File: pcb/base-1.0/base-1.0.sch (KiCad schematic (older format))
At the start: 80 parts, among them J101 USB_B_Micro, J102 UART, J103 74984104400, J104 Jack-DC, J105 USB_GPIO, J106 Raspberry_Pi_2_3, Q101 BC817, Q102 BC817, Q103 DMP2305U-7, SW101 SW_Push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

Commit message: o Finding more components. o Refreshing generated files.
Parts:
- Q101, Q102: mpn (none) -> BC817,235
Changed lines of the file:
@@
 F 2 "Package_TO_SOT_SMD:SOT-23" H 9200 2225 50  0001 L CIN
 F 3 "https://assets.nexperia.com/documents/data-sheet/BC817_SER.pdf" H 9000 2300 50  0001 L CNN
+F 4 "BC817,235" H 9000 2300 50  0001 C CNN "mpn"
 	1    9000 2300
 	1    0    0    1
@@
 F 2 "Package_TO_SOT_SMD:SOT-23" H 9200 1525 50  0001 L CIN
 F 3 "https://assets.nexperia.com/documents/data-sheet/BC817_SER.pdf" H 9000 1600 50  0001 L CNN
+F 4 "BC817,235" H 9000 1600 50  0001 C CNN "mpn"
 	1    9000 1600
 	1    0    0    -1

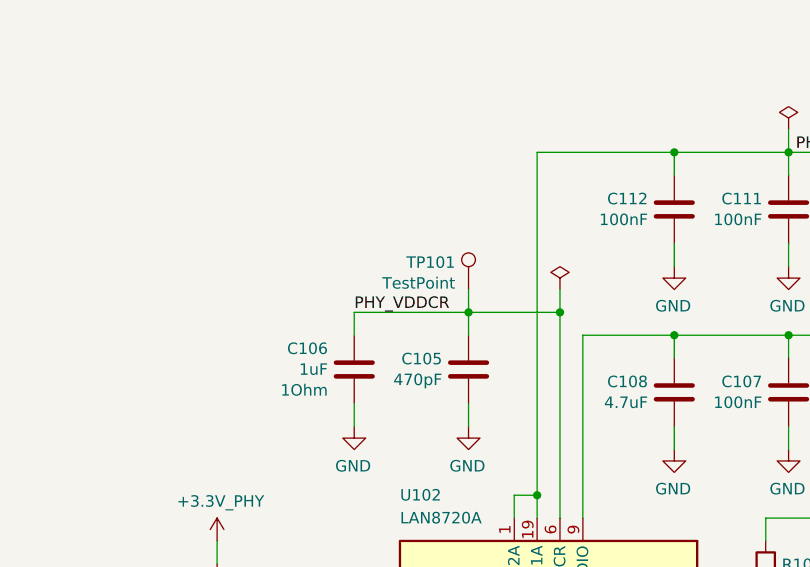
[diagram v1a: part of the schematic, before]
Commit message: o Selecting more parts, fixing footprints.
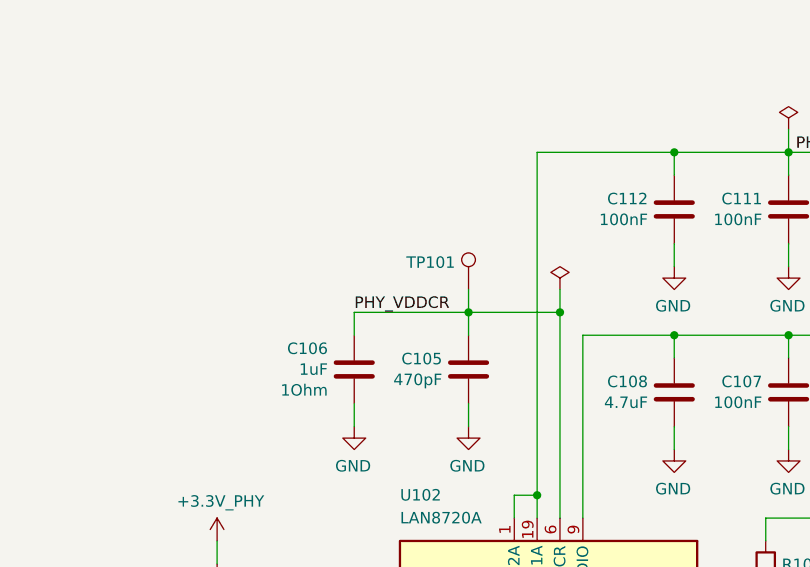
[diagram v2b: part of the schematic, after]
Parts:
- C104: footprint IPC-7351-CAPC:CAPC_1005x015 -> IPC-7351-CAPC:CAPC_4532x040
- C120, C121: footprint IPC-7351-CAPC:CAPC_1005x015 -> IPC-7351-CAPC:CAPC_2012x040
- FB101, FB102: mpn (none) -> FBMJ2125HS250NT
- TP101: value TestPoint -> PHY_VDDCR
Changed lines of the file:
@@
 F 0 "C104" H 2015 10841 50  0000 L CNN
 F 1 "1nF" H 2015 10750 50  0000 L CNN
-F 2 "IPC-7351-CAPC:CAPC_1005x015" H 1938 10600 50  0001 C CNN
+F 2 "IPC-7351-CAPC:CAPC_4532x040" H 1938 10600 50  0001 C CNN
 F 3 "~" H 1900 10750 50  0001 C CNN
 F 4 "2kV" H 2015 10659 50  0000 L CNN "Voltage"
@@
 Wire Wire Line
 	6000 7700 6000 7600
-$Comp
-L Connector:TestPoint TP101
-U 1 1 5DDF6049
-P 4600 7400
-F 0 "TP101" H 4658 7518 50  0000 L CNN
-F 1 "TestPoint" H 4658 7427 50  0000 L CNN
-F 2 "TestPoint:TestPoint_Pad_1.5x1.5mm" H 4800 7400 50  0001 C CNN
-F 3 "~" H 4800 7400 50  0001 C CNN
-	1    4600 7400
-	-1   0    0    -1
-$EndComp
 Connection ~ 4600 7500
 Wire Wire Line
@@
 F 4 "2A" V 6850 6800 50  0001 C CNN "I"
 F 5 "50mOhm" V 6850 6800 50  0001 C CNN "DCR"
+F 6 "FBMJ2125HS250NT" V 6850 6800 50  0001 C CNN "mpn"
 	1    6850 6800
 	0    -1   1    0
@@
 F 2 "Inductor_SMD:L_0402_1005Metric" V 1330 1200 50  0001 C CNN
 F 3 "~" H 1400 1200 50  0001 C CNN
+F 4 "FBMJ2125HS250NT" V 1400 1200 50  0001 C CNN "mpn"
 	1    1400 1200
 	0    1    1    0
@@
 F 0 "C120" H 13215 6441 50  0000 L CNN
 F 1 "100nF" H 13215 6350 50  0000 L CNN
-F 2 "IPC-7351-CAPC:CAPC_1005x015" H 13138 6200 50  0001 C CNN
+F 2 "IPC-7351-CAPC:CAPC_2012x040" H 13138 6200 50  0001 C CNN
 F 3 "" H 13100 6350 50  0000 C CNN
 F 4 "C3" H 13100 6350 50  0001 C CNN "ta_ref"
@@
 F 0 "C121" H 13215 8541 50  0000 L CNN
 F 1 "100nF" H 13215 8450 50  0000 L CNN
-F 2 "IPC-7351-CAPC:CAPC_1005x015" H 13138 8300 50  0001 C CNN
+F 2 "IPC-7351-CAPC:CAPC_2012x040" H 13138 8300 50  0001 C CNN
 F 3 "" H 13100 8450 50  0000 C CNN
 F 4 "C3" H 13100 8450 50  0001 C CNN "ta_ref"
@@
 	0    1    -1   0
 $EndComp
+$Comp
+L Connector:TestPoint TP101
+U 1 1 5DDF6049
+P 4600 7400
+F 0 "TP101" H 4658 7518 50  0000 L CNN
+F 1 "PHY_VDDCR" H 4658 7427 50  0001 L CNN
+F 2 "TestPoint:TestPoint_Pad_1.5x1.5mm" H 4800 7400 50  0001 C CNN
+F 3 "~" H 4800 7400 50  0001 C CNN
+	1    4600 7400
+	-1   0    0    -1
+$EndComp
 $EndSCHEMATC

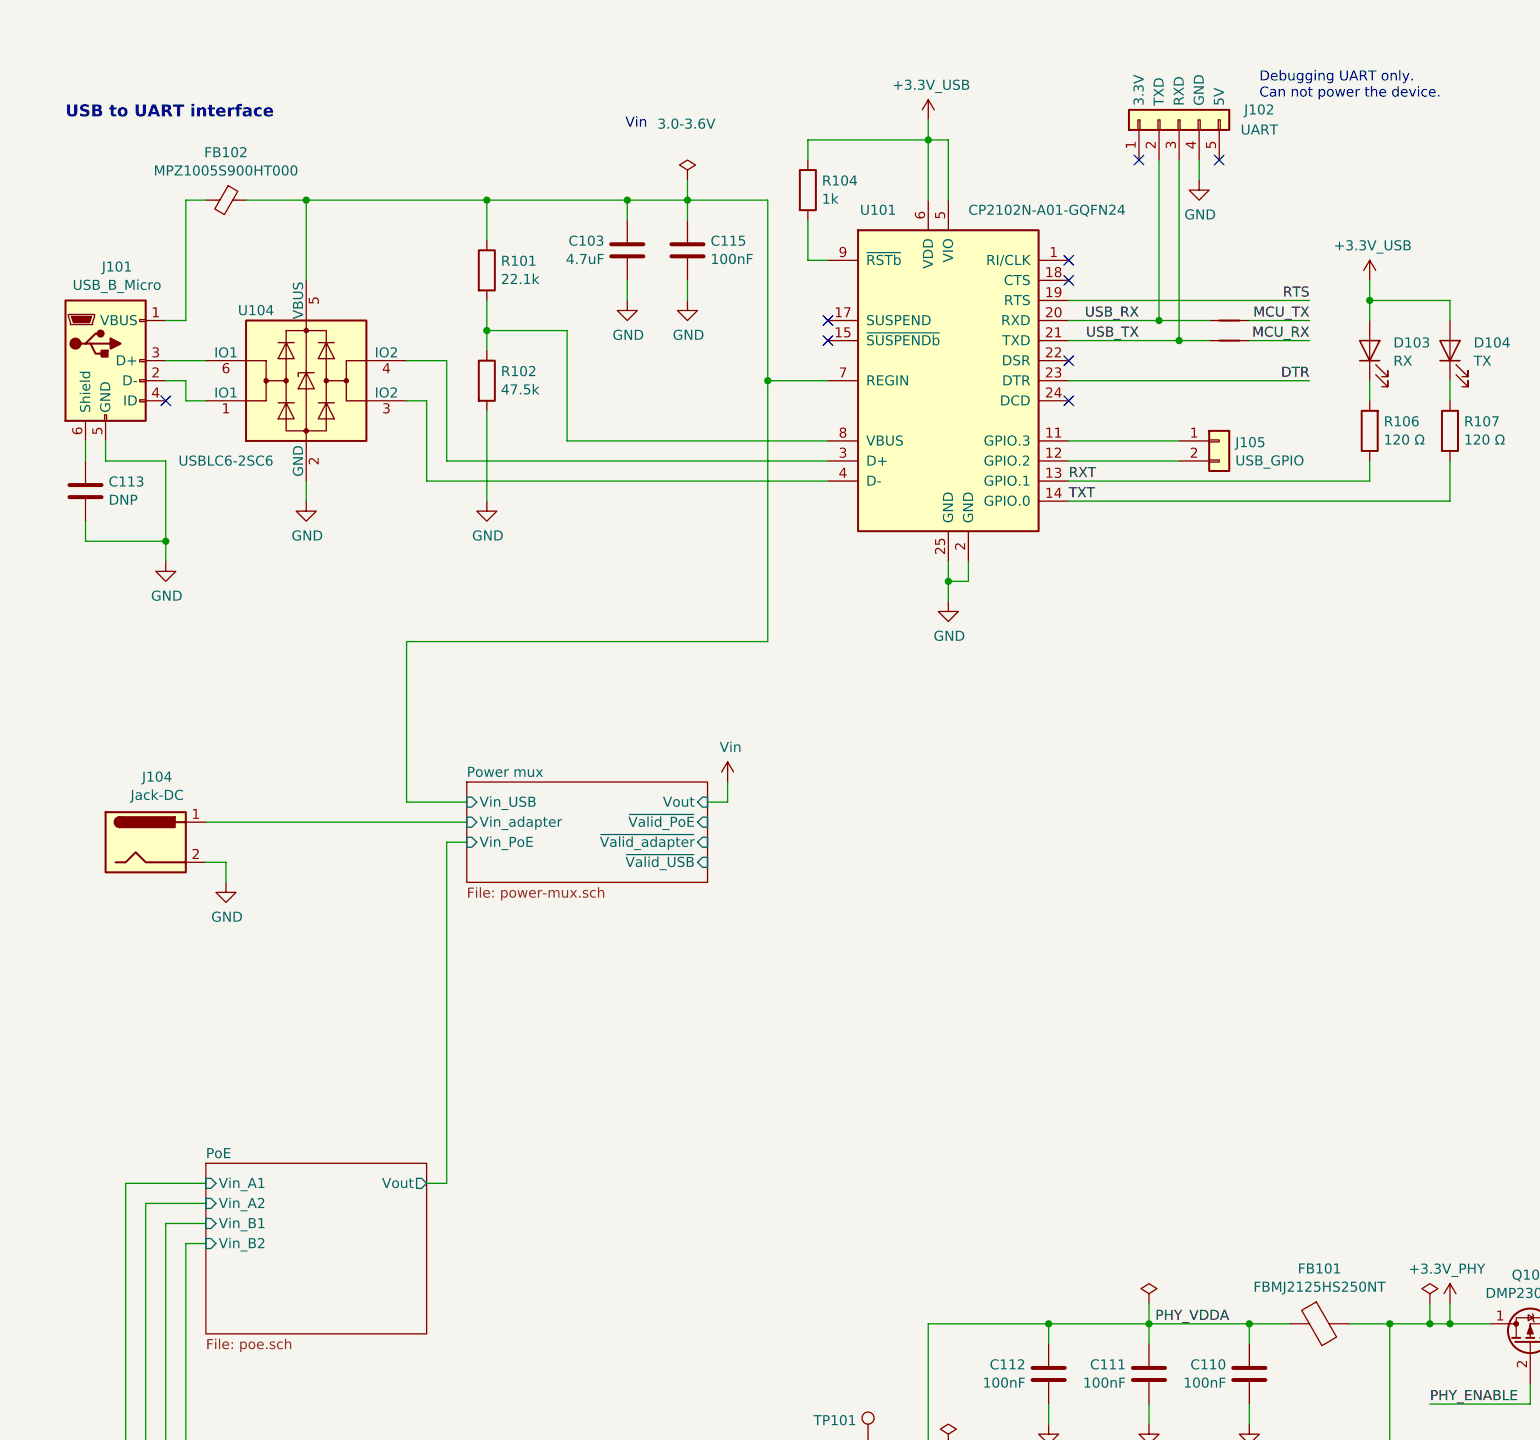
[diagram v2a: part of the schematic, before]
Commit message: o Improving footprints.
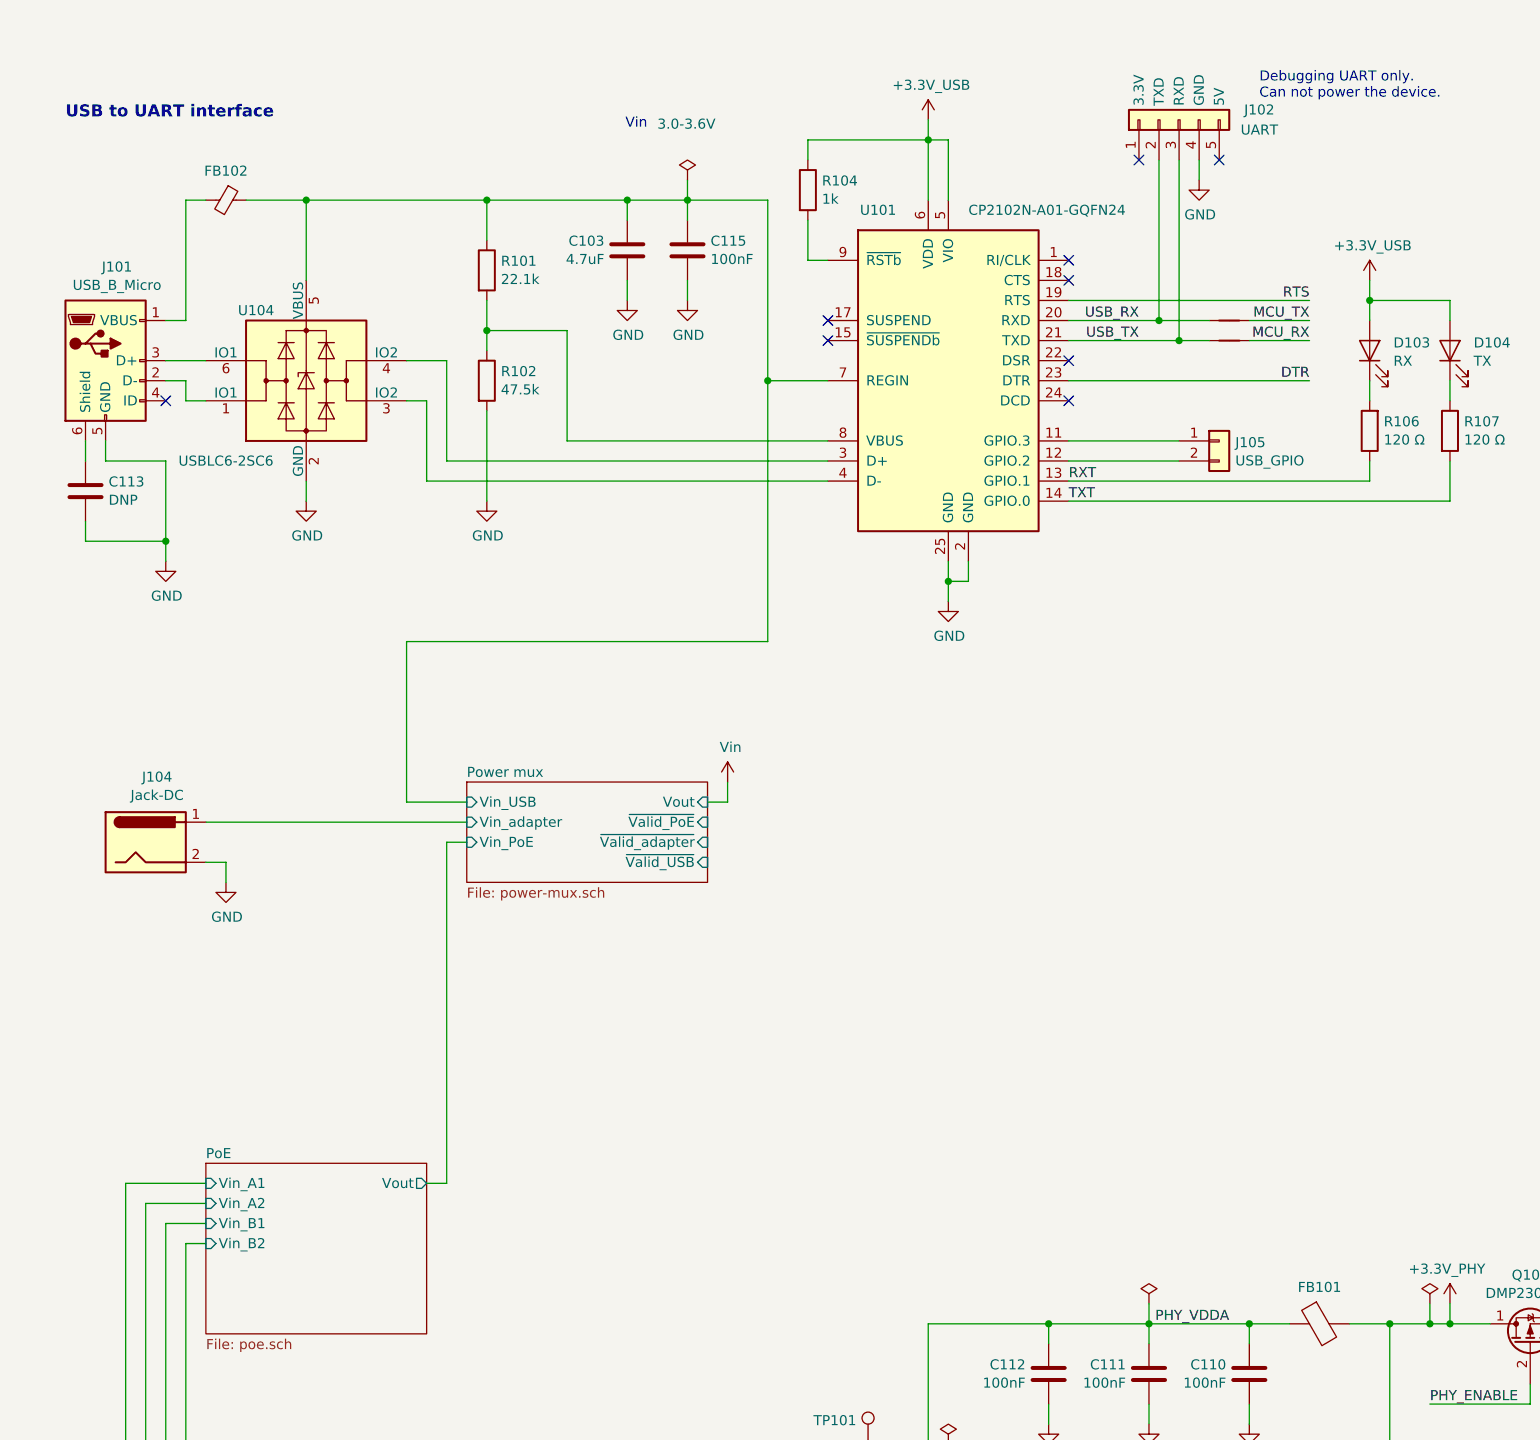
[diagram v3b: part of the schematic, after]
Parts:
- FB102: value MPZ1005S900HT000 -> FBMJ2125HS250NT; footprint Inductor_SMD:L_0402_1005Metric -> Inductor_SMD:L_0805_2012Metric
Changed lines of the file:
@@
 U 1 1 5D1E7600
 P 6850 6800
-F 0 "FB101" V 6576 6800 50  0000 C CNN
-F 1 "FBMJ2125HS250NT" V 6667 6800 50  0000 C CNN
+F 0 "FB101" V 6668 6800 50  0000 C CNN
+F 1 "FBMJ2125HS250NT" V 6667 6800 50  0001 C CNN
 F 2 "Inductor_SMD:L_0805_2012Metric" V 6780 6800 50  0001 C CNN
 F 3 "~" H 6850 6800 50  0001 C CNN
@@
 U 1 1 5CEB3AD9
 P 1400 1200
-F 0 "FB102" V 1163 1200 50  0000 C CNN
-F 1 "MPZ1005S900HT000" V 1254 1200 50  0000 C CNN
-F 2 "Inductor_SMD:L_0402_1005Metric" V 1330 1200 50  0001 C CNN
+F 0 "FB102" V 1255 1200 50  0000 C CNN
+F 1 "FBMJ2125HS250NT" V 1254 1200 50  0001 C CNN
+F 2 "Inductor_SMD:L_0805_2012Metric" V 1330 1200 50  0001 C CNN
 F 3 "~" H 1400 1200 50  0001 C CNN
 F 4 "FBMJ2125HS250NT" V 1400 1200 50  0001 C CNN "mpn"

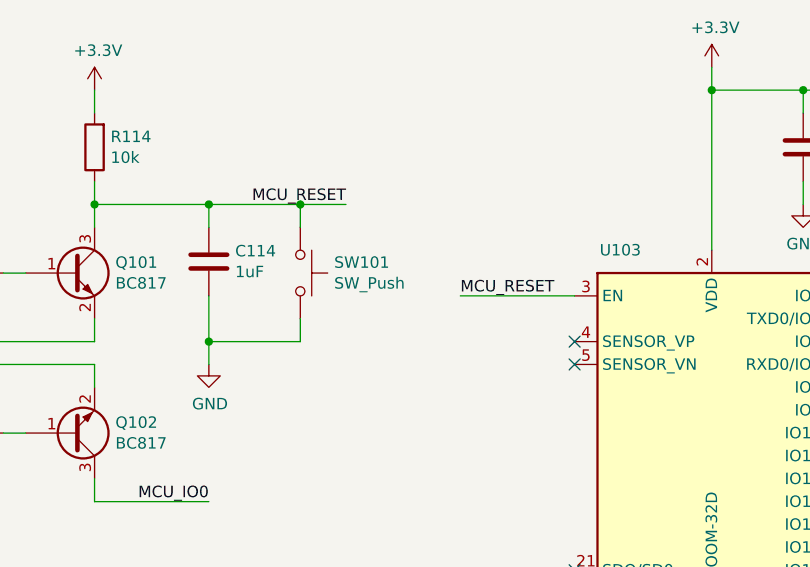
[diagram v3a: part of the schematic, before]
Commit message: o More footprints and mpns.
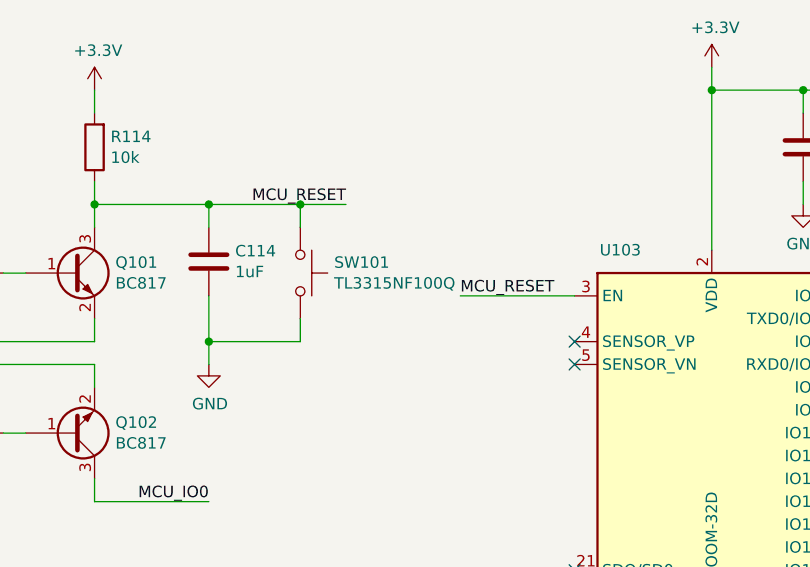
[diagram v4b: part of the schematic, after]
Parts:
- J106: mpn (none) -> PPPC202LFBN-RC
- L102: Imin NRS8040T220MJGJ -> 2A; mpn (none) -> NRS8040T220MJGJ
- SW101: value SW_Push -> TL3315NF100Q
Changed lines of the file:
@@
 F 2 "Connector_PinHeader_2.54mm:PinHeader_2x20_P2.54mm_Vertical" H 15000 2800 50  0001 C CNN
 F 3 "https://www.raspberrypi.org/documentation/hardware/raspberrypi/schematics/rpi_SCH_3bplus_1p0_reduced.pdf" H 15000 2800 50  0001 C CNN
+F 4 "PPPC202LFBN-RC" H 15000 2800 50  0001 C CNN "mpn"
 	1    15000 2800
 	1    0    0    -1
@@
 P 10000 1600
 F 0 "SW101" V 9954 1748 50  0000 L CNN
-F 1 "SW_Push" V 10045 1748 50  0000 L CNN
+F 1 "TL3315NF100Q" V 10045 1748 50  0000 L CNN
 F 2 "TL3315:TL3315" H 10000 1800 50  0001 C CNN
 F 3 "~" H 10000 1800 50  0001 C CNN
@@
 F 3 "https://ds.yuden.co.jp/TYCOMPAS/ut/detail?pn=NRS8040T220MJGJ%20%20&u=M" H 13550 8700 50  0001 C CNN
 F 4 "L1" V 13550 8700 50  0001 C CNN "ta_ref"
-F 5 "NRS8040T220MJGJ" V 13550 8700 50  0001 C CNN "Imin"
+F 5 "2A" V 13550 8700 50  0001 C CNN "Imin"
+F 6 "NRS8040T220MJGJ" V 13550 8700 50  0001 C CNN "mpn"
 	1    13550 8700
 	0    1    -1   0

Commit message: o Adding IO extender for RPI header. o Adding mounting holes in schematic and PCB. o Fixing bad footprint: Capacitor_SMD:CP_Elec_8x10.2 => Capacitor_SMD:CP_Elec_8x10.
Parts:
- added C128: 100nF, IPC-7351-CAPC:CAPC_2012x040, symbol Device:C
- added H101, H102, H103, H104: MountingHole, MountingHole:MountingHole_2.5mm, symbol Mechanical:MountingHole
- added U107: MCP23S17, Package_DFN_QFN:QFN-28-1EP_6x6mm_P0.65mm_EP4.25x4.25mm, symbol Interface_Expansion:MCP23S17_ML
- J106: value Raspberry_Pi_2_3 -> RPI_HEADER
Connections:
- net PHY_ENABLE is gone; now on net MCU_IO15: Q103.2 (G)
- net +3V3: now also J106.1 (3V3), J106.17 (3V3), C128.1, U107.5 (VDD)
- net GND: now also C128.2, U107.11 (A0), U107.12 (A1), U107.13 (A2), U107.29 (EP), U107.6 (VSS)
- net MCU_RESET: now also U107.14 (~RESET~)
- net MCU_RX: now also J106.10 (GPIO15/RXD)
- net MCU_TX: now also J106.8 (GPIO14/TXD)
- net MCU_IO14: now reaches U103.13 (IO14)
- net MCU_IO14: now also J106.40 (GPIO21/SCLK1)
- net MCU_IO12: now reaches U103.14 (IO12)
- net MCU_IO12: now also J106.3 (SDA/GPIO2)
- net MCU_IO13: now reaches U103.16 (IO13)
- net MCU_IO13: now also J106.5 (SCL/GPIO3)
- net MCU_IO15: now reaches U103.23 (IO15)
- net MCU_IO2: now reaches U103.24 (IO2)
- net MCU_IO2: now also J106.12 (GPIO18/PWM0)
- net MCU_IO4: now reaches U103.26 (IO4)
- net MCU_IO4: now also J106.32 (PWM0/GPIO12)
- net MCU_IO16: now reaches U103.27 (IO16)
- net MCU_IO16: now also U107.9 (SI)
- net MCU_IO5: now reaches U103.29 (IO5)
- net MCU_IO5: now also J106.33 (PWM1/GPIO13)
- net MCU_IO34: now reaches U103.6 (IO34)
- net MCU_IO34: now also U107.16 (INTA)
- net MCU_IO35: now reaches U103.7 (IO35)
- net MCU_IO35: now also U107.10 (SO)
- net MCU_IO32: now reaches U103.8 (IO32)
- net MCU_IO32: now also U107.7 (~CS~)
- net MCU_IO33: now reaches U103.9 (IO33)
- net MCU_IO33: now also U107.8 (SCK)
- net EXP_B1: now reaches J106.11 (GPIO17)
- net EXP_B1: now also U107.26 (GPB1)
- net EXP_B7: now reaches J106.13 (GPIO27)
- net EXP_B7: now also U107.4 (GPB7)
- net EXP_B2: now reaches J106.15 (GPIO22)
- net EXP_B2: now also U107.27 (GPB2)
- net EXP_B3: now reaches J106.16 (GPIO23)
- net EXP_B3: now also U107.28 (GPB3)
- net EXP_B4: now reaches J106.18 (GPIO24)
- net EXP_B4: now also U107.1 (GPB4)
- net EXP_A7: now reaches J106.21 (MISO0/GPIO9)
- net EXP_A7: now also U107.24 (GPA7)
- net EXP_B5: now reaches J106.22 (GPIO25)
- net EXP_B5: now also U107.2 (GPB5)
- net EXP_A6: now reaches J106.24 (~CE0~/GPIO8)
- net EXP_A6: now also U107.23 (GPA6)
- net EXP_A5: now reaches J106.26 (~CE1~/GPIO7)
- net EXP_A5: now also U107.22 (GPA5)
- net EXP_A0: now reaches J106.27 (ID_SD/GPIO0)
- net EXP_A0: now also U107.17 (GPA0)
- net EXP_A1: now reaches J106.28 (ID_SC/GPIO1)
- net EXP_A1: now also U107.18 (GPA1)
- net EXP_A3: now reaches J106.29 (GCLK1/GPIO5)
- net EXP_A3: now also U107.20 (GPA3)
- net EXP_A4: now reaches J106.31 (GCLK2/GPIO6)
- net EXP_A4: now also U107.21 (GPA4)
- net EXP_B0: now reaches J106.36 (GPIO16)
- net EXP_B0: now also U107.25 (GPB0)
- net EXP_B6: now reaches J106.37 (GPIO26)
- net EXP_B6: now also U107.3 (GPB6)
- net EXP_A2: now reaches J106.7 (GCLK0/GPIO4)
- net EXP_A2: now also U107.19 (GPA2)
- no-connect marks 21 -> 28
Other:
- moved on the sheet: C101, C102, C114, C116, C117, C118, C119, C120, C121, C122, C123, C124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

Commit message: o Much more PCB work.
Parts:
- removed RN101: R_Network04, Resistor_THT:R_Array_SIP5, symbol Device:R_Network04
- added RN101: 49.9 Ω, Resistor_SMD:R_Array_Convex_4x1206, symbol Device:R_Pack04
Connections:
- net +3V3_PHY: now also RN101.5 (R4.2), RN101.6 (R3.2), RN101.7 (R2.2), RN101.8 (R1.2)
- net ETH_RD+: now also RN101.1 (R1.1)
- net ETH_RD-: now also RN101.2 (R2.1)
- net ETH_TD+: now also RN101.3 (R3.1)
- net ETH_TD-: now also RN101.4 (R4.1)
- net D+: now reaches U101.3 (D+), U104.4 (IO2)
- net D-: now reaches U101.4 (D-), U104.3 (IO2)
- net at J101.2 (D-): now also U104.6 (IO1); no longer U104.1 (IO1)
- net at J101.3 (D+): now also U104.1 (IO1); no longer U104.6 (IO1)
- net BOOT renamed BOOT_12V
- net BOOT_12V: no longer C120.1, U105.6 (BOOT)
- net FB renamed FB_12V
- net FB_12V: no longer C122.2, R103.2, R105.1, U105.4 (FB)
- net SW renamed SW_12V
- net SW_12V: no longer C120.2, L101.2, U105.2 (SW)
- new net BOOT_3.3V: C120.1, U105.6 (BOOT)
- new net FB_3.3V: C122.2, R103.2, R105.1, U105.4 (FB)
- new net SW_3.3V: C120.2, L101.2, U105.2 (SW)
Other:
- note added: "TODO: Connect to connector's shield"
- note added: "TODO: Move big capacitors outside of the switch"
- moved on the sheet: C113, C120, C121, C122, C123, C124, C125, C126, C127, D101, D102, J101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
